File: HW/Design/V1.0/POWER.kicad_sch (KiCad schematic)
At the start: 44 parts, among them J1 9V-12V, J2 USB C, Q1 SI2301, Q3 SI2301, Q4 2N3906, U1 LDO 3.3V/300mA, U2 MT1470, U3 MT3608

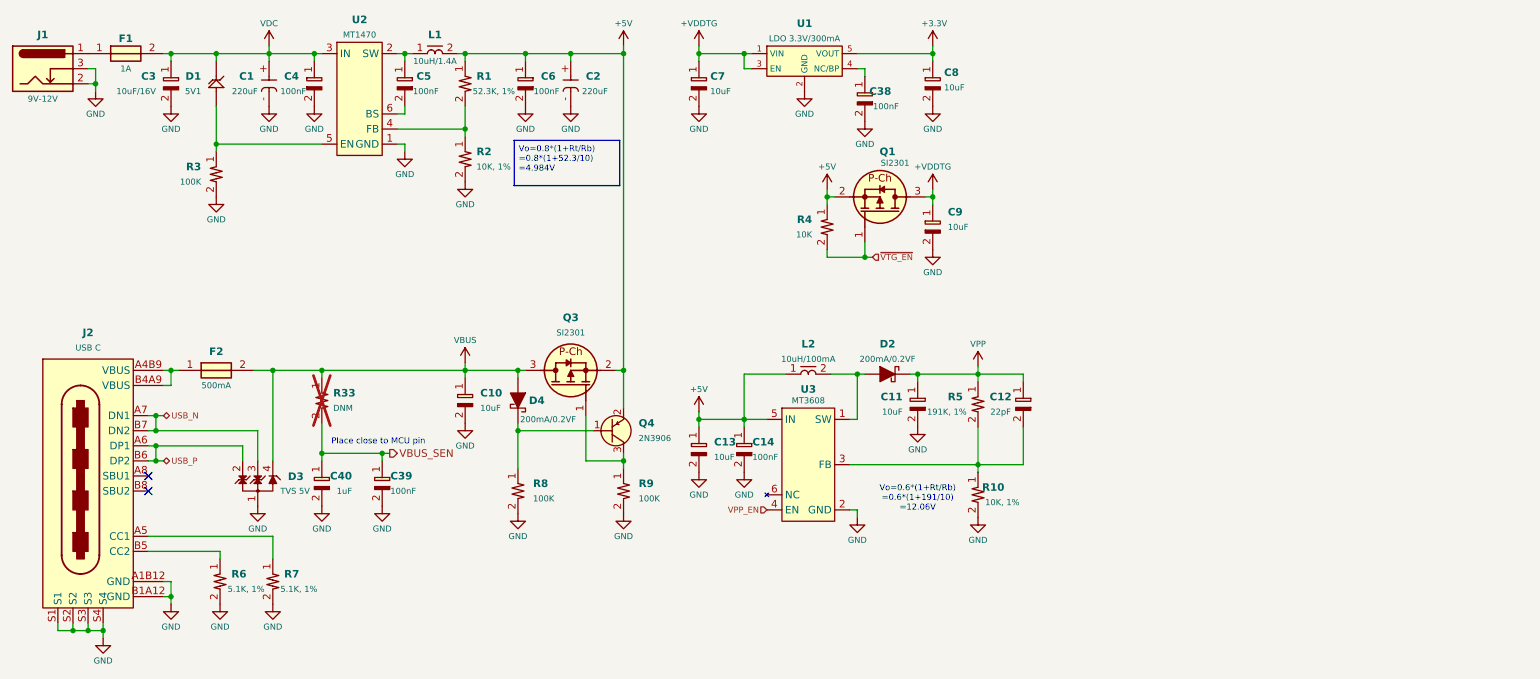
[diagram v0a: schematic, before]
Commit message: PCB V2: change programmer MCU
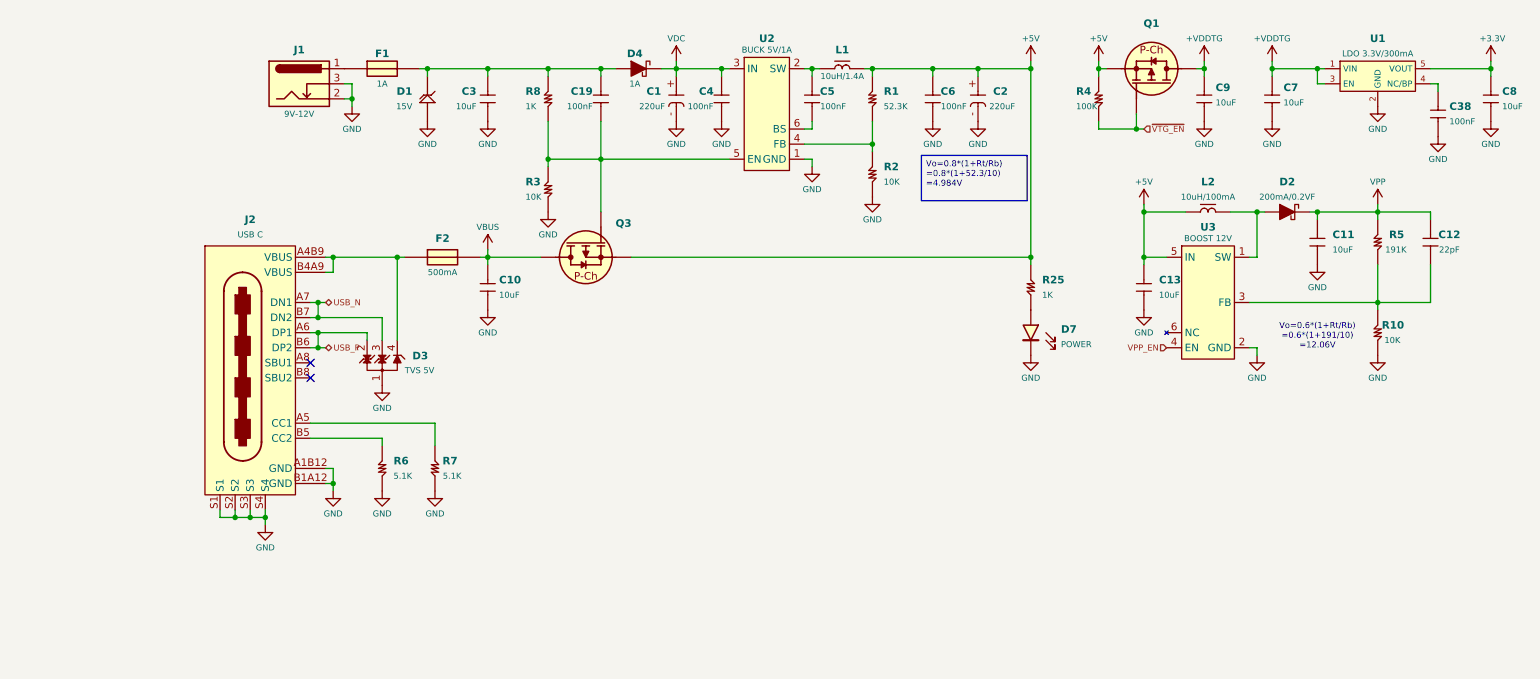
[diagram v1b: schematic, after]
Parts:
- removed C14, C39: 100nF, SAMPI:CAP0603, symbol Triet_KiCAD_Sym:CAP_CER
- removed C40: 1uF, SAMPI:CAP0603, symbol Triet_KiCAD_Sym:CAP_CER
- removed Q4: 2N3906, SAMPI:SOT23, symbol SAMPI:BJT-PNP
- removed R33: DNM, SAMPI:RES0603, symbol Triet_KiCAD_Sym:RES
- removed R8, R9: 100K, SAMPI:RES0603, symbol Triet_KiCAD_Sym:RES
- added C19: 100nF, SAMPI:CAP0603, symbol SAMPI:CERCAP
- added D7: POWER, SAMPI:LED0603, symbol Triet_KiCAD_Sym:LED
- added R25, R8: 1K, SAMPI:RES0603, symbol SAMPI:RES
- C10, C11, C12, C13, C38, C4, C5, C6, C7, C8, C9: symbol Triet_KiCAD_Sym:CAP_CER -> SAMPI:CERCAP
- C3: value 10uF/16V -> 10uF; symbol Triet_KiCAD_Sym:CAP_CER -> SAMPI:CERCAP
- D1: value 5V1 -> 15V; footprint SAMPI:SOD80C-LL34 -> SAMPI:DO-214AC; MFT Diotec -> Shenzhen; MNP ZMM5.1R13 -> SMAJ15A
- D4: value 200mA/0.2VF -> 1A; footprint SAMPI:SOD-123FL -> SAMPI:DO-214AC; MFT Vishay -> MDD; MNP BAT43W-E3-08 -> SS24
- R1: value 52.3K, 1% -> 52.3K; symbol Triet_KiCAD_Sym:RES -> SAMPI:RES
- R10, R2: value 10K, 1% -> 10K; symbol Triet_KiCAD_Sym:RES -> SAMPI:RES
- R3: value 100K -> 10K; symbol Triet_KiCAD_Sym:RES -> SAMPI:RES
- R4: value 10K -> 100K; symbol Triet_KiCAD_Sym:RES -> SAMPI:RES
- R5: value 191K, 1% -> 191K; symbol Triet_KiCAD_Sym:RES -> SAMPI:RES
- R6, R7: value 5.1K, 1% -> 5.1K; symbol Triet_KiCAD_Sym:RES -> SAMPI:RES
- U2: value MT1470 -> BUCK 5V/1A
- U3: value MT3608 -> BOOST 12V
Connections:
- net +3.3V: now also C8.2; no longer C8.1
- net +5V: now also C13.2, R1.2, R25.2; no longer C13.1, R1.1
- net +VDDTG: now also C7.2, C9.2; no longer C7.1, C9.1
- net GND: now also C10.1, C13.1, C4.1, C7.1, C8.1, C9.1, D1.A, R2.1, R7.1, D7.K; no longer C10.2, C13.2, C4.2, C7.2, C8.2, C9.2, R2.2, R7.2
- net VBUS: now also C10.2; no longer C10.1, D3.4 (CH3), D4.A
- net VDC: now also C4.2, D4.K; no longer C3.1, C4.1, D1.K, F1.2
- net at J2.A5 (CC1): now also R7.2; no longer R7.1
- net at Q3.1 (G): now also R3.1, U2.5 (EN), C19.1, R8.2
- net at F2.1, J2.A4B9 (VBUS), J2.B4A9 (VBUS): now also D3.4 (CH3)
- new net: D7.A, R25.1
- new net: C19.2, C3.1, D1.K, D4.A, F1.2, R8.1
- new net: R1.1, R2.2, U2.4 (FB)
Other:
- note removed: "Place close to MCU pin"
- moved on the sheet: C1, C2, D1, D2, D3, J1, J2, U1, U2, U3
